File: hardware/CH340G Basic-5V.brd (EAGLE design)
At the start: 22.9 x 16.5 mm, 24 parts, among them J1 microB, U1 AP2112-3.3V, U2 CH340G, Y2 12MHz

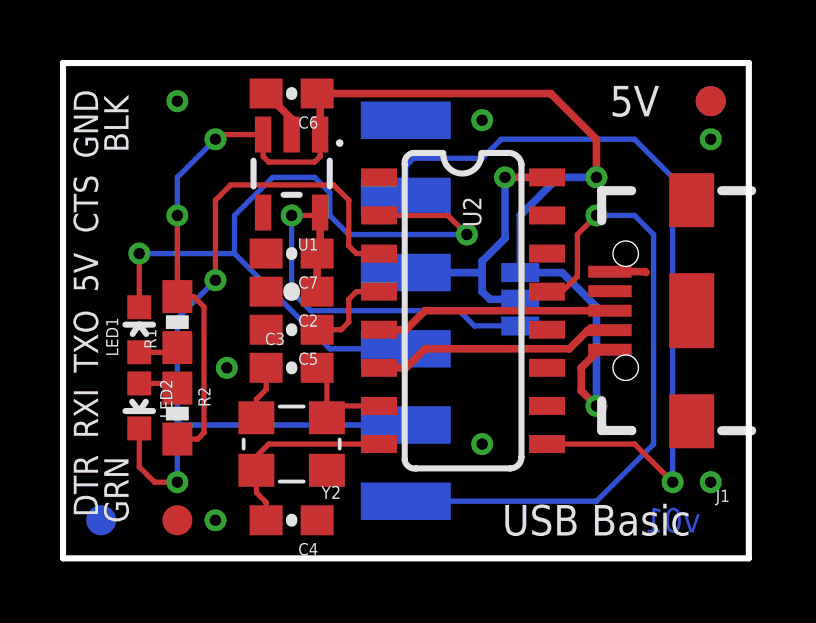
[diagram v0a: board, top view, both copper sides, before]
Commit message: Added TP to 3.3V. Passes checklist.
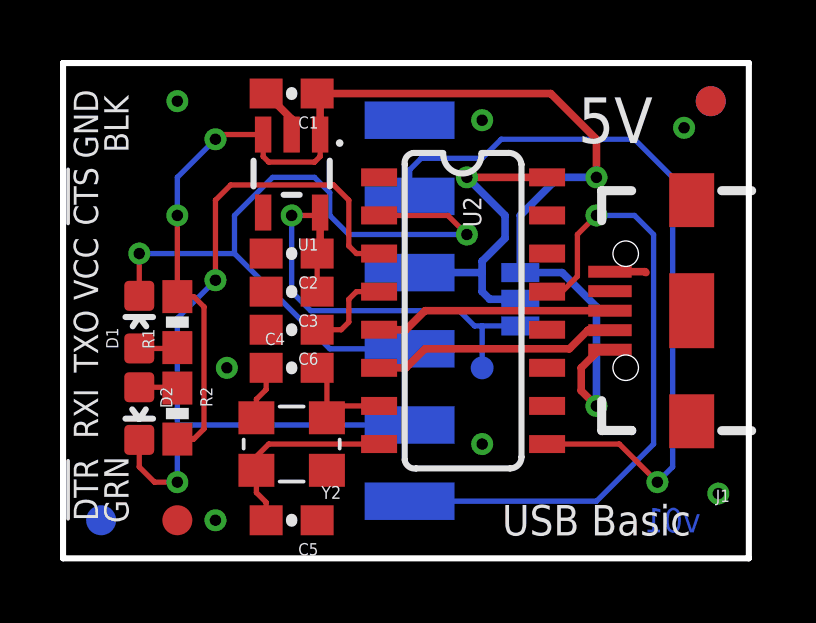
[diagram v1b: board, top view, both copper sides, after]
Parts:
- removed C7: 1.0uF, SparkFun-Capacitors:0603-CAP
- removed JP1: (no value), SparkFun:1X06-SMD-FEMALE-V2
- removed LED1: Red, SparkFun:LED-0603
- removed LED2: Green, SparkFun:LED-0603
- added C1: 1.0uF, SparkFun-Capacitors:0603-CAP
- added D1: GREEN, SparkFun-LED:LED-0603
- added D2: Yellow, SparkFun-LED:LED-0603
- added J3: (no value), SparkFun-Connectors:1X06-SMD-FEMALE-V2
- added TP1: 3.3V TP, SparkFun-Passives:PAD.03X.03
- C2: value 0.1uF -> 1.0uF; device SparkFun:0603-CAP -> SparkFun-Capacitors:0603-CAP
- C3: value 10pF -> 0.1uF
- C5: value 10nF -> 10pF
- C6: value 1.0uF -> 10nF
- R1, R2: device SparkFun:0603-RES -> SparkFun-Resistors:0603-RES
- moved C6 7.87 mm to (7.62, 7.62)
- moved C5 6.35 mm to (7.62, 1.27)
- moved C4 5.08 mm to (7.62, 6.35), turned to 0 degrees
- moved C3 2.54 mm to (7.62, 8.89), turned to 180 degrees
- moved C2 1.27 mm to (7.62, 10.2)
- renumbered SJ2 to SJ1
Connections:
- removed net POWER: JP1.3, SJ1.2, U2.16
- new net VCC: J3.3, SJ1.2, U2.16
- net !CTS: now also J3.2; no longer JP1.2
- net !DTR: now also J3.6; no longer JP1.6
- net 3.3V: now also C3.1, TP1.P$1; no longer C7.1
- net 5V: now also C1.1; no longer C6.1
- net GND: now also C1.2, C3.2, C5.1, J3.1; no longer C3.1, C5.2, C7.2, JP1.1
- net N$1: now also D1.A; no longer LED1.A
- net N$2: now also D2.A; no longer LED2.A
- net N$3: now also C5.2; no longer C4.2
- net N$4: now also C4.2; no longer C3.2
- net RXI: now also D2.C, J3.5; no longer JP1.5, LED2.C
- net TXO: now also D1.C, J3.4; no longer JP1.4, LED1.C
- net V3: now also C6.1; no longer C5.1
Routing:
- net VCC: track 0.00 -> 11.1 mm, vias 0 -> 1
- net POWER: track 9.45 -> 0.00 mm, vias 1 -> 0
- net 3.3V: track 14.3 -> 15.7 mm
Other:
- board text added: "!CTS"
- board text added: "!DTR"
- board text added: "VCC"
- board text removed: "CTS"
- board text removed: "DTR"
